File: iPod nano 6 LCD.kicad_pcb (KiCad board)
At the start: 2 copper layers, 40 x 40 mm, 80 parts, among them J1 Molex_503548-1220, J2 USB_C_Receptacle_USB2.0, J3 Conn_01x06_Male, U1 AP5724, U2 ICE40HX1K-TQ144, U3 TLV62569DBV, U4 TLV62569DBV, U5 XTSD04GLGEAG, U6 TLV62569DBV, U7 AT25xxx

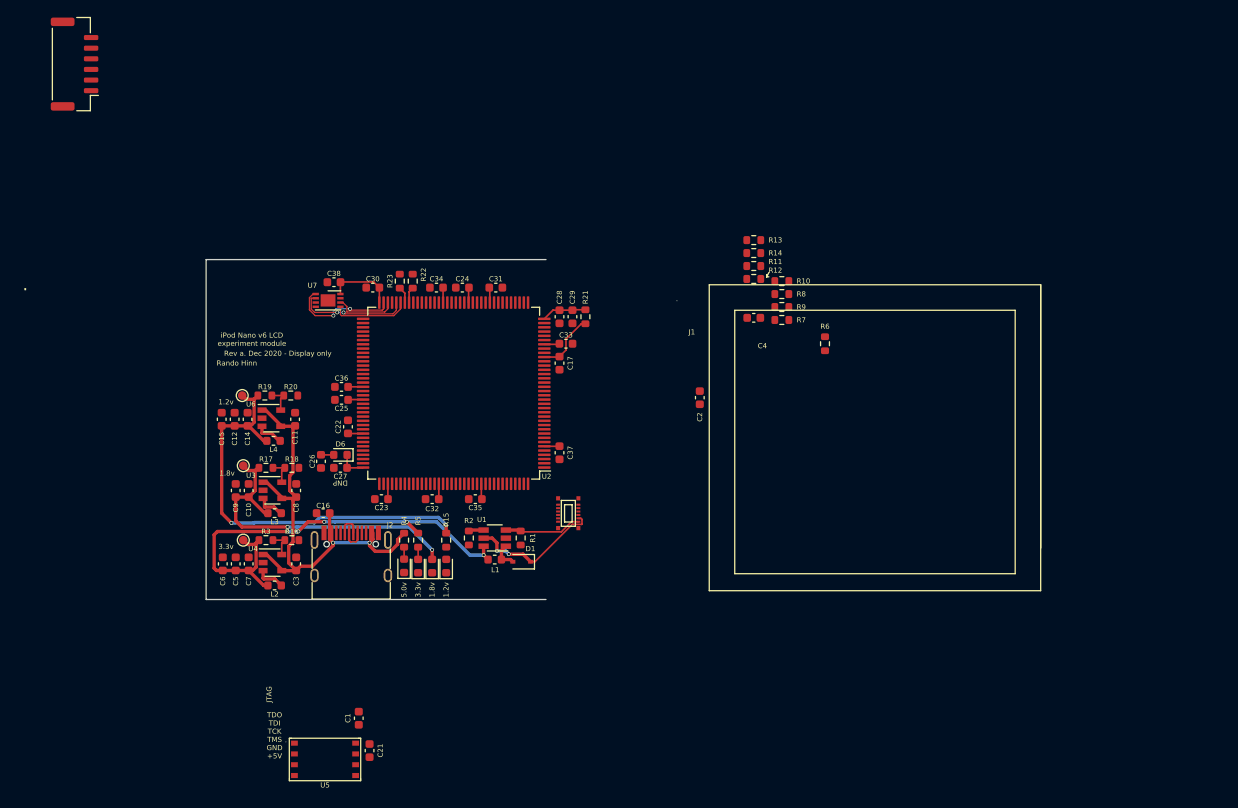
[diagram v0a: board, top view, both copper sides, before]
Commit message: Add LCD differential pairs, user led and reset/user butons, connect SD module CS pin to FPGA
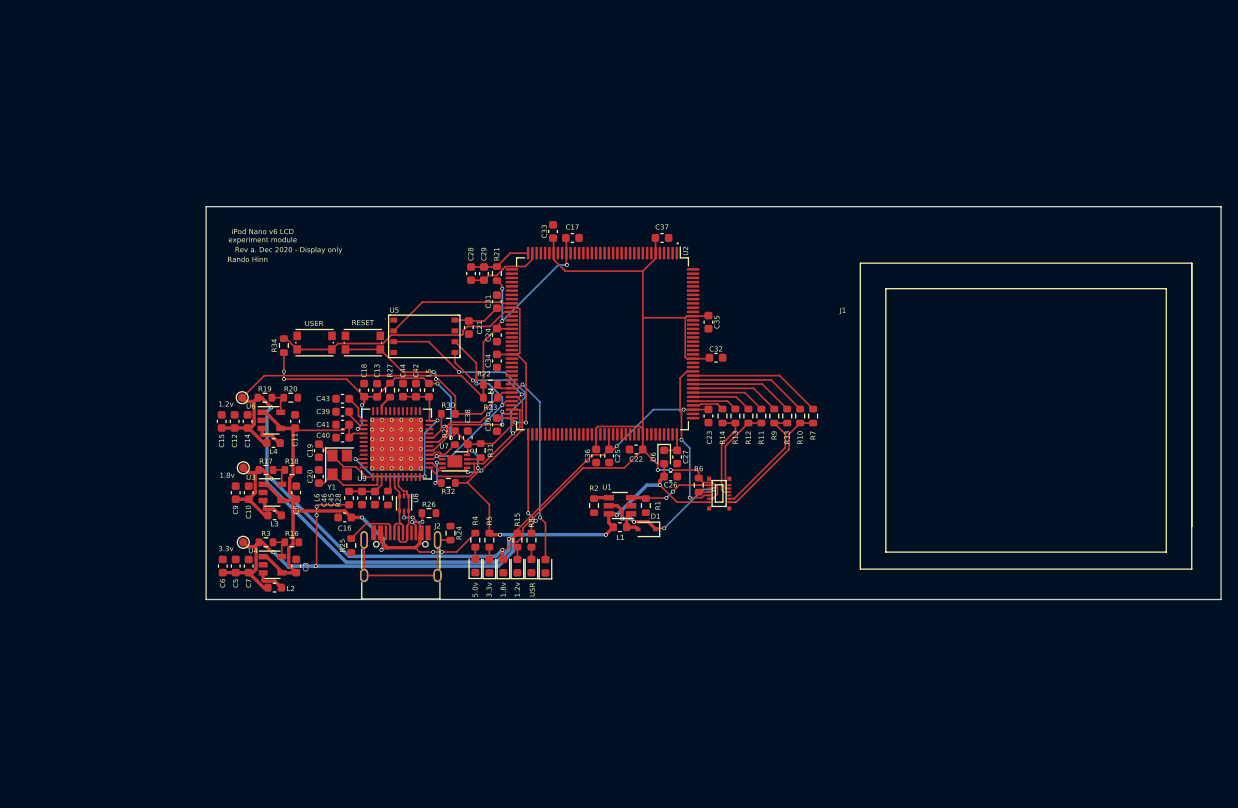
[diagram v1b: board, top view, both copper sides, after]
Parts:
- removed C1, C2, C4: 1u, Capacitor_SMD:C_0603_1608Metric
- removed J3: Conn_01x06_Male, Connector_JST:JST_GH_BM06B-GHS-TBT_1x06-1MP_P1.25mm_Vertical
- added C13: 100n, Capacitor_SMD:C_0603_1608Metric, F.Cu at (137.9, 73.2)
- added C18: 4.7u, Capacitor_SMD:C_0603_1608Metric, F.Cu at (136.4, 73.2)
- added C19: 10p, Capacitor_SMD:C_0603_1608Metric, F.Cu at (131.1, 80.3)
- added C20: 10p, Capacitor_SMD:C_0603_1608Metric, F.Cu at (131.1, 83.3)
- added C39: 100n, Capacitor_SMD:C_0603_1608Metric, F.Cu at (133.9, 75.7)
- added C40: 100n, Capacitor_SMD:C_0603_1608Metric, F.Cu at (133.9, 78.7)
- added C41: 4.7u, Capacitor_SMD:C_0603_1608Metric, F.Cu at (133.9, 77.2)
- added C42: 4.7u, Capacitor_SMD:C_0603_1608Metric, F.Cu at (142.5, 73.2)
- added C43: 100n, Capacitor_SMD:C_0603_1608Metric, F.Cu at (133.9, 74.2)
- added C44: 100n, Capacitor_SMD:C_0603_1608Metric, F.Cu at (141.0, 73.2)
- added C45: 4.7u, Capacitor_SMD:C_0603_1608Metric, F.Cu at (137.7, 85.9)
- added C46: 100n, Capacitor_SMD:C_0603_1608Metric, F.Cu at (136.1, 85.9)
- added D7: USR, LED_SMD:LED_0603_1608Metric, F.Cu at (156.1, 93.9)
- added D8: USR, LED_SMD:LED_0603_1608Metric, F.Cu at (157.7, 93.9)
- added L5: 600, Inductor_SMD:L_0603_1608Metric, F.Cu at (144.0, 73.2)
- added L6: 600, Inductor_SMD:L_0603_1608Metric, F.Cu at (134.6, 85.9)
- added R24: 1M, Resistor_SMD:R_0603_1608Metric, F.Cu at (146.6, 90.0)
- added R25: 5.1k, Resistor_SMD:R_0603_1608Metric, F.Cu at (134.9, 91.4)
- added R26: 5.1k, Resistor_SMD:R_0603_1608Metric, F.Cu at (144.0, 87.6)
- added R27: 12k, Resistor_SMD:R_0603_1608Metric, F.Cu at (139.4, 73.2)
- added R28: 12k, Resistor_SMD:R_0603_1608Metric, F.Cu at (139.2, 85.9)
- added R29: 10k, Resistor_SMD:R_0603_1608Metric, F.Cu at (147.1, 78.7)
- added R30: 2k2, Resistor_SMD:R_0603_1608Metric, F.Cu at (146.3, 75.9)
- added R31: 10k, Resistor_SMD:R_0603_1608Metric, F.Cu at (150.1, 80.3)
- added R32: 10k, Resistor_SMD:R_0603_1608Metric, F.Cu at (146.3, 84.1)
- added R33: 220, Resistor_SMD:R_0603_1608Metric, F.Cu at (186.2, 76.2)
- added R34: 10k, Resistor_SMD:R_0603_1608Metric, F.Cu at (126.9, 67.9)
- added SW1: SW_Push, Button_Switch_SMD:SW_Push_1P1T_NO_CK_KMR2, F.Cu at (136.2, 67.6)
- added SW2: SW_Push, Button_Switch_SMD:SW_Push_1P1T_NO_CK_KMR2, F.Cu at (130.6, 67.6)
- added U8: USBLC6-2P6, Package_TO_SOT_SMD:SOT-666, F.Cu at (141.1, 86.5)
- added U9: FT232H, Package_DFN_QFN:QFN-48-1EP_8x8mm_P0.5mm_EP6.2x6.2mm_ThermalVias, F.Cu at (140.2, 79.5)
- added Y1: 12MHz, Crystal:Crystal_SMD_Abracon_ABM8G-4Pin_3.2x2.5mm, F.Cu at (133.5, 82.0)
- R8: value 220 -> 8
- moved C21 51.1 mm to (148.7, 65.8)
- moved U5 51.1 mm to (143.5, 66.9)
- moved R8 41.3 mm to (156.1, 90.8), turned to 270 degrees
- moved C26 41.2 mm to (172.5, 83.3), turned to 0 degrees
- moved C23 39.7 mm to (176.9, 76.2), turned to 270 degrees
- moved C27 39.6 mm to (173.2, 81.0), turned to 270 degrees
- moved D6 38.1 mm to (171.7, 81.0), turned to 270 degrees
- moved C32 37.3 mm to (177.8, 69.3)
- moved C35 34.4 mm to (176.9, 65.2), turned to 90 degrees
- moved C22 34.0 mm to (168.4, 80.1), turned to 0 degrees
- moved C25 32.2 mm to (165.2, 80.9), turned to 270 degrees
- moved C36 31.1 mm to (163.7, 80.9), turned to 90 degrees
- moved C37 28.0 mm to (171.4, 55.2), turned to 180 degrees
- moved C38 24.1 mm to (148.6, 78.7), turned to 270 degrees
- moved U7 24.1 mm to (147.1, 81.5)
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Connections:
- net Net-(J2-PadA6) renamed /USBD_P
- net Net-(J2-PadA7) renamed /USBD_N
- net Net-(R22-Pad1) renamed /ICE_DONE
- net Net-(R23-Pad1) renamed /ICE_CRESET
- C21 pad 2: VDDIN -> +3V3
- C26 pad 1: VDDIN -> +3V3
- C30 pad 1: VDDIN -> +3V3
- C31 pad 2: VDDIN -> +3V3
- C32 pad 2: VDDIN -> +1V8
- C34 pad 2: VDDIN -> +3V3
- C35 pad 2: VDDIN -> +1V8
- C38 pad 2: VDDIN -> +3V3
- C5 pad 1: VDDIN -> +3V3
- C6 pad 1: VDDIN -> +3V3
- C7 pad 1: VDDIN -> +3V3
- D6 pad 2: VDDIN -> +3V3
- J1 pad 1: CLKP -> /LCD_CP
- J1 pad 2: VDDIN -> +3V3
- J1 pad 3: CLKN -> /LCD_CN
- J1 pad 6: SYNC -> /VSYNC
- J1 pad 7: DP -> /LCD_DP
- J1 pad 9: DN -> /LCD_DN
- J2 pad S1: GND -> Net-(J2-PadS1)
- L1 pad 1: VDDIN -> +3V3
- L2 pad 2: VDDIN -> +3V3
- R10 pad 1: Net-(R10-Pad1) -> /LCD_CP
- R10 pad 2: CLKP -> /ICE_CP
- R11 pad 1: Net-(R11-Pad1) -> /LCD_DN
- R11 pad 2: DN -> /ICE_DNBIAS
- R12 pad 1: Net-(R12-Pad1) -> /LCD_DN
- R12 pad 2: DN -> /ICE_DN
- R13 pad 1: Net-(R13-Pad1) -> /ICE_DPBIAS
- R13 pad 2: DP -> /LCD_DP
- R14 pad 1: Net-(R14-Pad1) -> /LCD_DP
- R14 pad 2: DP -> /ICE_DP
- R3 pad 1: VDDIN -> +3V3
- R5 pad 1: VDDIN -> +3V3
- R7 pad 1: IC_CLKN -> /ICE_CPBIAS
- R7 pad 2: CLKN -> /LCD_CP
- R8 pad 1: IC_CLKP -> /USR_LED
- R8 pad 2: CLKP -> Net-(D7-Pad2)
- R9 pad 1: Net-(R9-Pad1) -> /LCD_CN
- R9 pad 2: CLKN -> /ICE_CN
- TP2 pad 1: VDDIN -> +3V3
- U1 pad 6: VDDIN -> +3V3
- U2 pad 112: Net-(U2-Pad112) -> /ICE_DP
- U2 pad 113: Net-(U2-Pad113) -> /ICE_DPBIAS
- U2 pad 114: Net-(U2-Pad114) -> /ICE_DN
- U2 pad 115: Net-(U2-Pad115) -> /ICE_DNBIAS
- U2 pad 116: Net-(U2-Pad116) -> /ICE_CN
- U2 pad 117: Net-(U2-Pad117) -> /ICE_CNBIAS
- U2 pad 118: Net-(U2-Pad118) -> /ICE_CP
- U2 pad 119: Net-(U2-Pad119) -> /ICE_CPBIAS
- U2 pad 120: Net-(U2-Pad120) -> /VSYNC
- U2 pad 123: VDDIN -> +1V8
- U2 pad 133: VDDIN -> +1V8
- U2 pad 45: Net-(U2-Pad45) -> SD_CS
- U2 pad 46: VDDIN -> +3V3
- U2 pad 57: VDDIN -> +3V3
- U2 pad 71: CFG_CS -> /ICE_SS_B
- U2 pad 72: VDDIN -> +3V3
- U2 pad 73: Net-(U2-Pad73) -> /USR_LED
- U5 pad 3: SCLK -> SCK
- U5 pad 8: VDDIN -> +3V3
- U7 pad 1: CFG_CS -> /CFG_CS
- U7 pad 8: VDDIN -> +3V3
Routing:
- net +3V3: track 0.00 -> 180.3 mm, vias 0 -> 18
- net +1V8: track 45.9 -> 143.3 mm, vias 2 -> 4
- net +1V2: track 63.0 -> 149.7 mm, vias 2 -> 7
- net VDDIN: track 71.6 -> 0.00 mm, vias 5 -> 0
- net /ICE_DONE: track 1.88 -> 37.7 mm, vias 0 -> 4
- net SCK: track 7.32 -> 41.7 mm, vias 0 -> 2
- net Net-(R34-Pad2): track 0.00 -> 29.4 mm
- net Net-(C42-Pad2): track 0.00 -> 24.6 mm, vias 0 -> 3
- net /ICE_CRESET: track 1.95 -> 25.3 mm, vias 0 -> 2
- net +5V: track 53.8 -> 76.5 mm, vias 2 -> 6
- net MOSI: track 9.12 -> 30.7 mm, vias 0 -> 4
- net /VSYNC: track 0.00 -> 18.8 mm, vias 0 -> 2
- net Net-(J2-PadS1): track 0.00 -> 18.5 mm
- net /ICE_CPBIAS: track 0.00 -> 15.8 mm
- net SD_CS: track 0.00 -> 15.4 mm
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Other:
- board size 40 x 40 mm -> 119.4 x 46.2 mm
- board text added: "RESET"
- board text added: "USER"
- board text added: "USR"
- board text removed: "DNP"
- board text removed: "JTAG"
- board text removed: "TDO TDI TCK TMS GND +5V"

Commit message: Nearly done with routing.
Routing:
- net GND: track 0.00 -> 75.9 mm, vias 0 -> 628
- net Net-(C45-Pad2): track 5.08 -> 12.9 mm, vias 0 -> 2
- net +1V2: track 149.7 -> 154.1 mm, vias 7 -> 14
- net +3V3: track 180.3 -> 184.5 mm, vias 18 -> 21
- net +5V: track 76.5 -> 78.9 mm
- net Net-(R34-Pad2): track 29.4 -> 30.9 mm, vias 0 -> 2
- net MOSI: track 30.7 -> 31.3 mm
- net Net-(J2-PadA5): track 6.26 -> 6.75 mm, vias 0 -> 2
- net MISO: track 25.1 -> 25.4 mm, vias 3 -> 4
- net +1V8: track 143.3 -> 143.1 mm, vias 4 -> 6
- net SD_CS: vias 0 -> 2
- net /USR_LED: vias 2 -> 3
- added copper zone on B.Cu, net GND
- added copper zone on F.Cu, net GND

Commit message: Debounce cap for user switch
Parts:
- added C1: 10u, Capacitor_SMD:C_0603_1608Metric, F.Cu at (130.7, 70.2)
- added R35: 10k, Resistor_SMD:R_0603_1608Metric, F.Cu at (142.8, 62.6)
- added R36: 10k, Resistor_SMD:R_0603_1608Metric, F.Cu at (144.4, 62.6)
- added R37: 10k, Resistor_SMD:R_0603_1608Metric, F.Cu at (145.9, 62.6)
- added R38: 10k, Resistor_SMD:R_0603_1608Metric, F.Cu at (141.3, 62.6)
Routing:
- net +3V3: track 184.5 -> 192.8 mm
- net MOSI: track 31.3 -> 37.7 mm
- net SCK: track 41.7 -> 46.2 mm
- net MISO: track 25.4 -> 30.0 mm
- net GND: track 75.9 -> 73.3 mm
- net SD_CS: track 15.4 -> 17.7 mm
- net Net-(C1-Pad1): track 30.9 -> 32.4 mm
- net /ICE_CRESET: vias 2 -> 4
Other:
- board text added: "DONE"

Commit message: Start schematic cleanup
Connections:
- J1 pad 8: Net-(J1-Pad8) -> /LCD_RESET
- R6 pad 2: Net-(J1-Pad8) -> /LCD_RESET
- U2 pad 121: Net-(U2-Pad121) -> /LCD_RESET
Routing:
- net /LCD_RESET: track 0.00 -> 18.2 mm, vias 0 -> 2
- net Net-(J1-Pad8): track 1.23 -> 0.00 mm

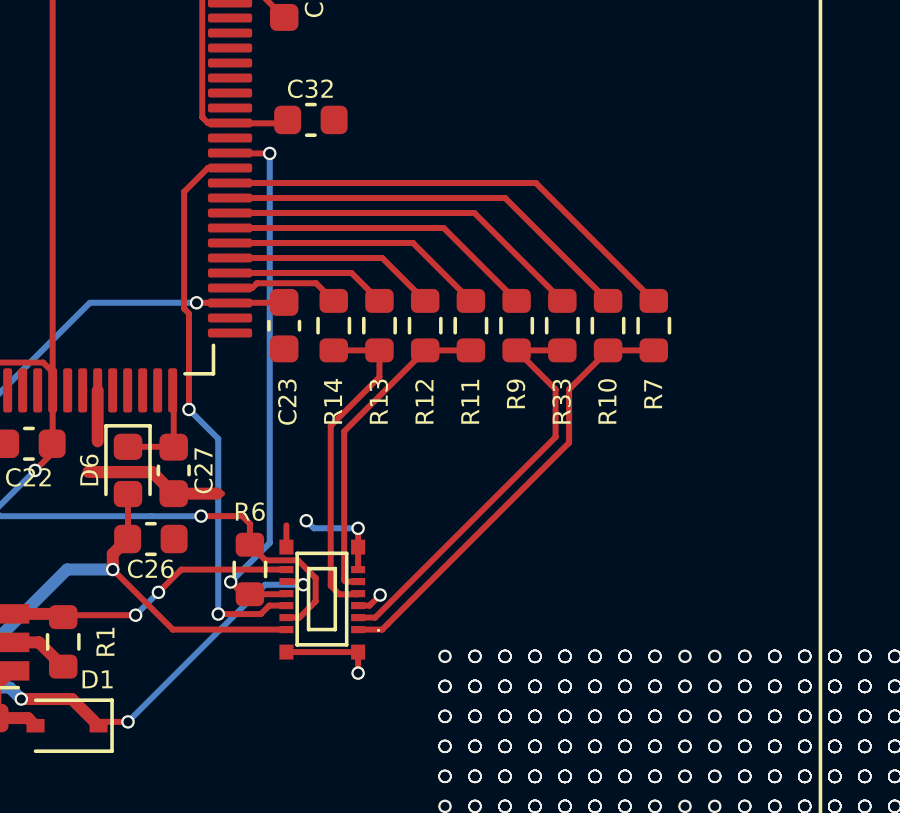
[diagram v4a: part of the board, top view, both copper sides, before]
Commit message: Adjust pin mapping a bit.
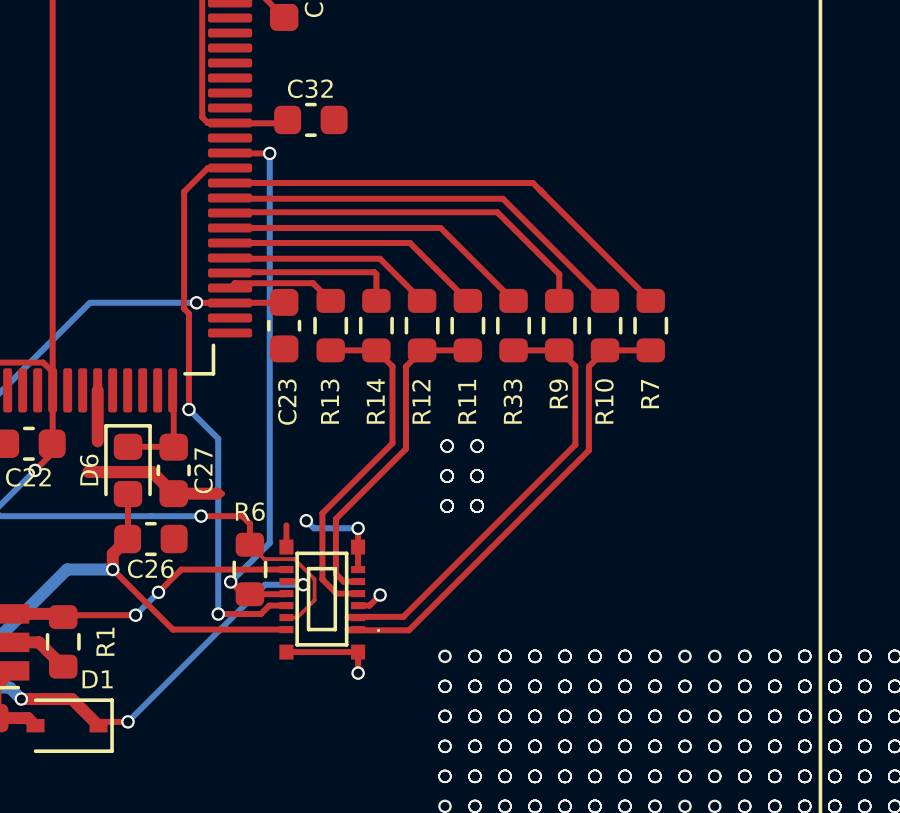
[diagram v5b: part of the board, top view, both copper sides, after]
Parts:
- moved R13 1.63 mm to (178.5, 76.2)
- moved R33 1.63 mm to (184.6, 76.2)
- moved R9 1.42 mm to (186.1, 76.2)
- moved R14 1.42 mm to (180.0, 76.2)
- moved R12 0.10 mm to (181.5, 76.2)
- moved R10 0.10 mm to (187.6, 76.2)
- moved R11 0.10 mm to (183.0, 76.2)
- moved R7 0.10 mm to (189.1, 76.2)
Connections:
- U2 pad 112: /ICE_DP -> /ICE_DPBIAS
- U2 pad 113: /ICE_DPBIAS -> /ICE_DP
- U2 pad 116: /ICE_CN -> /ICE_CNBIAS
- U2 pad 117: /ICE_CNBIAS -> /ICE_CN
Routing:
- net /ICE_CN: track 10.6 -> 12.7 mm
- net /ICE_DP: track 3.77 -> 5.80 mm
- net /ICE_CNBIAS: track 12.3 -> 10.5 mm
- net /ICE_DPBIAS: track 5.37 -> 3.66 mm
- net /LCD_CP: track 14.8 -> 16.0 mm
- net /LCD_CN: track 14.0 -> 15.2 mm
- net /LCD_DP: track 11.1 -> 11.7 mm
- net GND: vias 628 -> 663

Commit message: PCB
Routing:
- net GND: track 73.3 -> 64.7 mm, vias 663 -> 677
- net +1V8: track 143.0 -> 151.3 mm, vias 6 -> 7
- net +3V3: track 192.8 -> 198.4 mm, vias 21 -> 20
- net +1V2: track 154.1 -> 150.9 mm, vias 14 -> 13
- net /USBD_N: track 8.73 -> 10.2 mm
- net Net-(R32-Pad2): track 3.89 -> 2.69 mm
- net Net-(J2-PadB5): track 3.61 -> 2.61 mm, vias 2 -> 0
- net /ICE_CRESET: track 25.4 -> 26.4 mm
- net /ICE_SS_B: track 13.1 -> 12.1 mm, vias 2 -> 0
- net /ICE_DPBIAS: track 3.66 -> 4.55 mm
- net +5V: track 78.9 -> 79.8 mm
- net /ICE_DONE: track 37.7 -> 38.5 mm
- net Net-(L2-Pad1): track 3.38 -> 2.86 mm
- net MISO: track 30.0 -> 29.9 mm, vias 4 -> 3
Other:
- net class Default: clearance 0.0889 -> 0.127
- rule pad_to_mask_clearance: 0.051 -> 0
- rule trace_clearance: 0.0889 -> 0.127
